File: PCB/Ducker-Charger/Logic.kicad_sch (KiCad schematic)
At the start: 30 parts, among them IC1 TPS54202HDDCT, J3 Debug, U2 STM32F401RBT6, Y1 16MHz

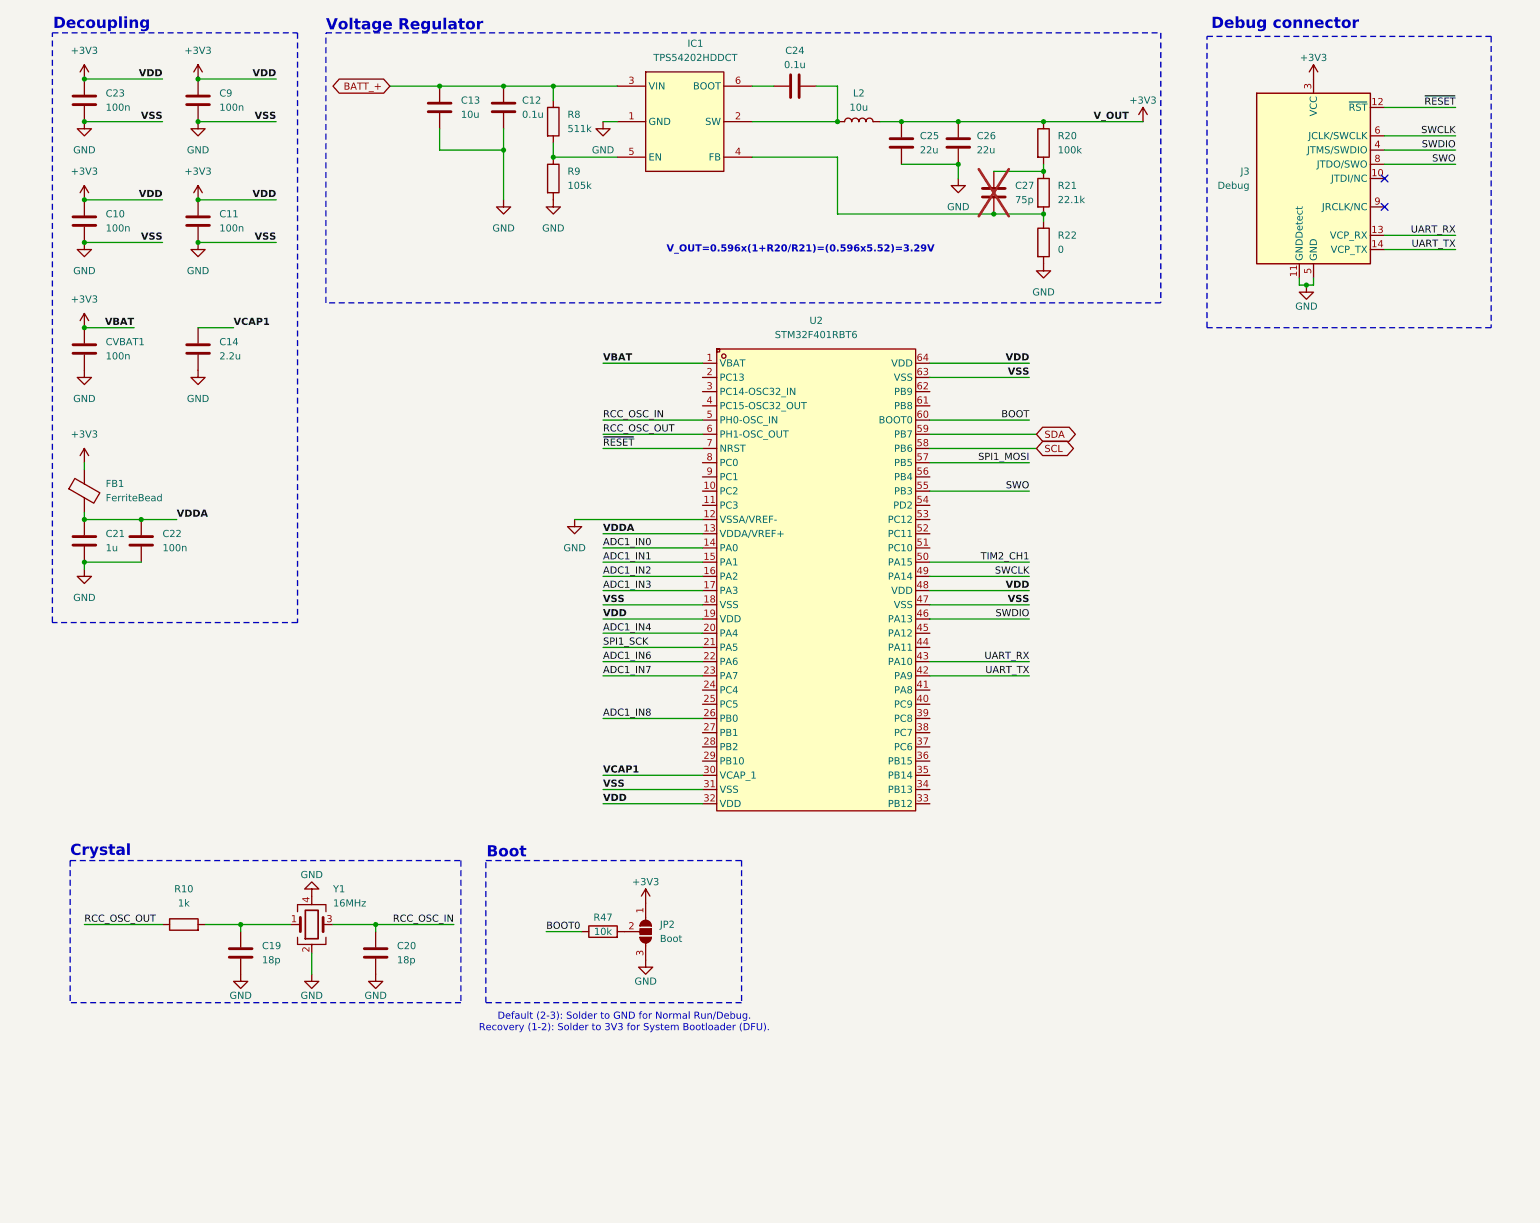
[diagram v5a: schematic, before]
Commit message: feat: progressed overall schematic
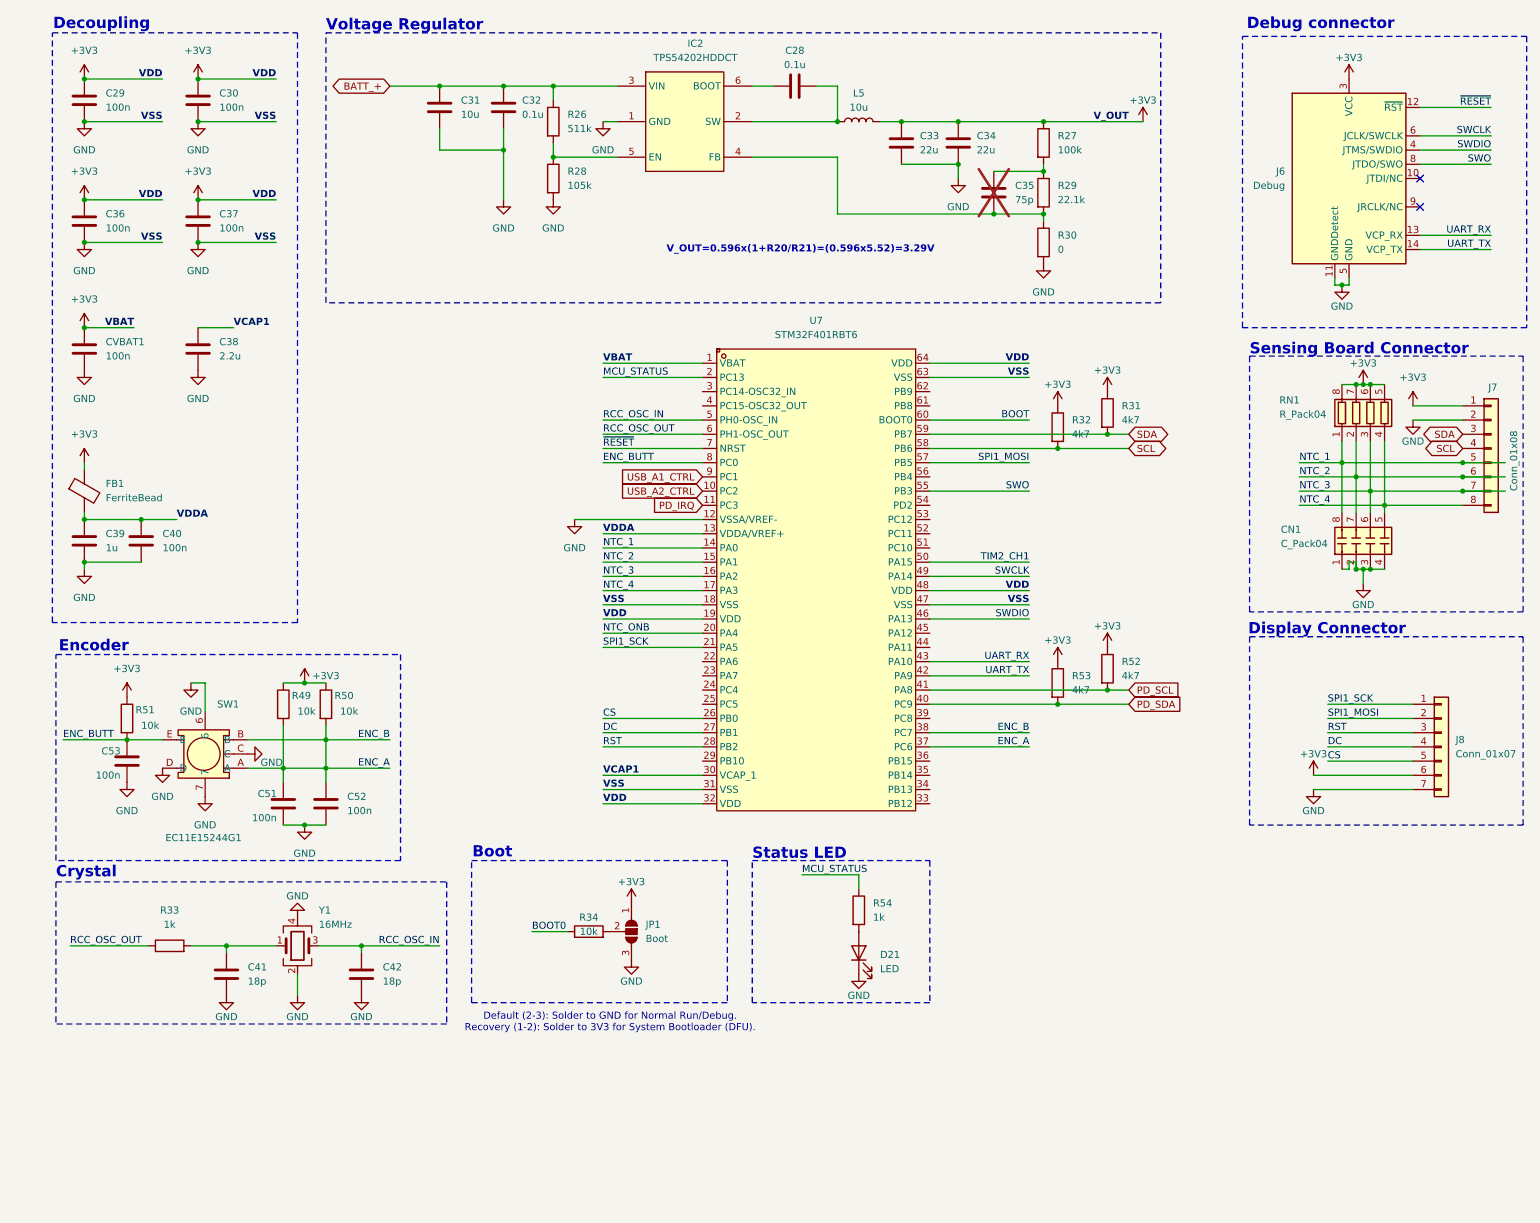
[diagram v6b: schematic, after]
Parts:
- added C51, C52, C53: 100n, symbol Device:C
- added CN1: C_Pack04, symbol Eagle_Main.:C_Pack04
- added D21: LED, LED_SMD:LED_0603_1608Metric, symbol Device:LED
- added J7: Conn_01x08, symbol Connector_Generic:Conn_01x08
- added J8: Conn_01x07, symbol Connector_Generic:Conn_01x07
- added R31, R32, R52, R53: 4k7, symbol Device:R
- added R49, R50, R51: 10k, symbol Device:R
- added R54: 1k, Resistor_SMD:R_0603_1608Metric, symbol Device:R
- added RN1: R_Pack04, symbol Device:R_Pack04
- added SW1: EC11E15244G1, EasyEDA:SW-TH_EC11E15244G1, symbol EasyEDA:EC11E15244G1
- IC2: renamed from IC1; footprint SOT95P280X110-6N -> TPS54202HDDCT:SOT95P280X110-6N
- renumbered C24 to C28, C23 to C29, C9 to C30, C13 to C31, C12 to C32, C25 to C33, C26 to C34, C27 to C35, C10 to C36, C11 to C37, C14 to C38, C21 to C39, C22 to C40, C19 to C41, C20 to C42, J3 to J6, JP2 to JP1, L2 to L5, R8 to R26, R20 to R27, R9 to R28, R21 to R29, R22 to R30, R10 to R33, R47 to R34, U2 to U7
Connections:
- net +3V3: now also J7.1 (Pin_1), J8.6 (Pin_6), R31.1, R32.1, R49.1, R50.1, R51.1, R52.1, R53.1, RN1.5 (R4.2), RN1.6 (R3.2), RN1.7 (R2.2), RN1.8 (R1.2)
- net GND: now also C51.2, C52.2, C53.2, CN1.1 (R1.1), CN1.2 (R2.1), CN1.3 (R3.1), CN1.4 (R4.1), D21.1 (K), J7.2 (Pin_2), J8.7 (Pin_7), SW1.6, SW1.7, SW1.C, SW1.D
- net SCL: now also J7.4 (Pin_4), R32.2
- net SDA: now also J7.3 (Pin_3), R31.2
- net SPI1_MOSI: now also J8.2 (Pin_2)
- net SPI1_SCK: now also J8.1 (Pin_1)
- net USB_A2_CTRL: now reaches U7.10 (PC2)
- net PD_IRQ: now reaches U7.11 (PC3)
- net MCU_STATUS: now reaches U7.2 (PC13)
- net MCU_STATUS: now also R54.1
- net DC: now reaches U7.27 (PB1)
- net DC: now also J8.4 (Pin_4)
- net RST: now reaches U7.28 (PB2)
- net RST: now also J8.3 (Pin_3)
- net ENC_A: now reaches U7.37 (PC6)
- net ENC_A: now also U7.38 (PC7), C51.1, C52.1, R49.2, R50.2, SW1.A, SW1.B
- net PD_SDA: now reaches U7.40 (PC9)
- net PD_SDA: now also R53.2
- net PD_SCL: now reaches U7.41 (PA8)
- net PD_SCL: now also R52.2
- net ENC_BUTT: now reaches U7.8 (PC0)
- net ENC_BUTT: now also C53.1, R51.2, SW1.E
- net USB_A1_CTRL: now reaches U7.9 (PC1)
- net ADC1_IN0 renamed NTC_1
- net NTC_1: now also CN1.8 (R1.2), J7.5 (Pin_5), RN1.1 (R1.1)
- net ADC1_IN1 renamed NTC_2
- net NTC_2: now also CN1.7 (R2.2), J7.6 (Pin_6), RN1.2 (R2.1)
- net ADC1_IN2 renamed NTC_3
- net NTC_3: now also CN1.6 (R3.2), J7.7 (Pin_7), RN1.3 (R3.1)
- net ADC1_IN3 renamed NTC_4
- net NTC_4: now also CN1.5 (R4.2), J7.8 (Pin_8), RN1.4 (R4.1)
- net ADC1_IN4 renamed NTC_ONB
- net ADC1_IN6: no longer names the net of U7.22 (PA6)
- net ADC1_IN7: no longer names the net of U7.23 (PA7)
- net ADC1_IN8 renamed CS
- net CS: now also J8.5 (Pin_5)
- new net: D21.2 (A), R54.2
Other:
- note added: "Display Connector"
- note added: "Encoder"
- note added: "Sensing Board Connector"
- note added: "Status LED"
- moved on the sheet: C41, C42, J6, JP1, R33, R34, Y1

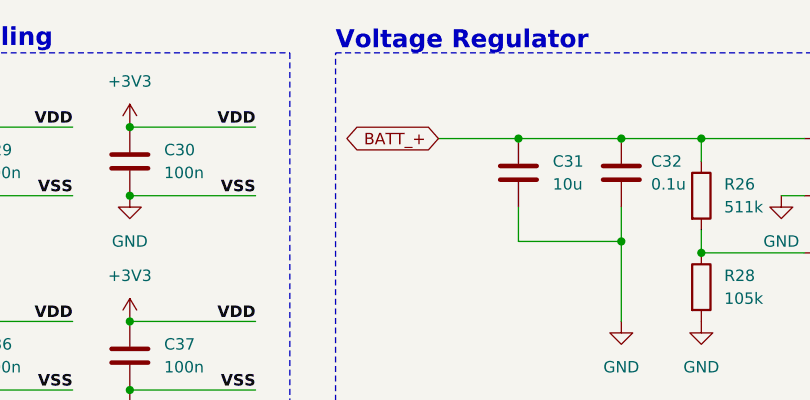
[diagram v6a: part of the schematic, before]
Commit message: fix: power symbols
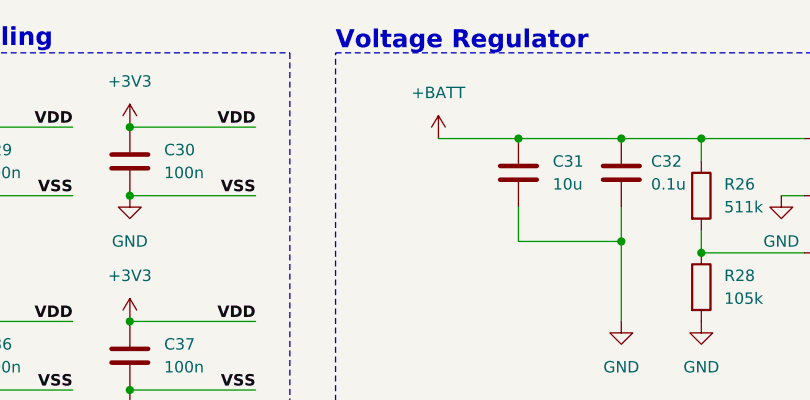
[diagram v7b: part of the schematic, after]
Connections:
- net BATT_+ renamed +BATT
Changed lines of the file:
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@@
 		)
 	)
-	(global_label "BATT_+"
-		(shape bidirectional)
-		(at 78.74 27.94 180)
-		(fields_autoplaced yes)
-		(effects
-			(font
-				(size 1.27 1.27)
-			)
-			(justify right)
-		)
-		(property "Intersheetrefs" "${INTERSHEET_REFS}"
-			(at 67.8097 27.94 0)
-			(effects
-				(font
-					(size 1.27 1.27)
-				)
-				(justify right)
-				(hide yes)
-			)
-		)
-	)
 	(global_label "PD_IRQ"
 		(shape input)
@@
 					(unit 1)
 				)
+			)
+		)
+	)
+	(symbol
+		(lib_id "power:+BATT")
+		(at 78.74 27.94 0)
+		(unit 1)
+		(exclude_from_sim no)
+		(in_bom yes)
+		(on_board yes)
+		(dnp no)
+		(fields_autoplaced yes)
+		(property "Reference" "#PWR0117"
+			(at 78.74 31.75 0)
+			(effects
+				(font
+					(size 1.27 1.27)
+				)
+				(hide yes)
+			)
+		)
+		(property "Value" "+BATT"
+			(at 78.74 22.86 0)
+			(effects
+				(font
+					(size 1.27 1.27)
+				)
+			)
+		)
+		(property "Footprint" ""
+			(at 78.74 27.94 0)
+			(effects
+				(font
+					(size 1.27 1.27)
+				)
+				(hide yes)
+			)
+		)
+		(property "Datasheet" ""
+			(at 78.74 27.94 0)
+			(effects
+				(font
+					(size 1.27 1.27)
+				)
+				(hide yes)
+			)
+		)
+		(property "Description" "Power symbol creates a global label with name \"+BATT\""
+			(at 78.74 27.94 0)
+			(effects
+				(font
+					(size 1.27 1.27)
+				)
+				(hide yes)
+			)
+		)
+		(pin "1"
+		)
+		(instances
+			(project "Ducker-Charger"
+				(path "/74790d6c-a68e-4e6d-b4a9-43de1843f817/b1375a06-d47d-478c-835c-6ba88db99bcf"
+					(reference "#PWR0117")
+					(unit 1)
+				)

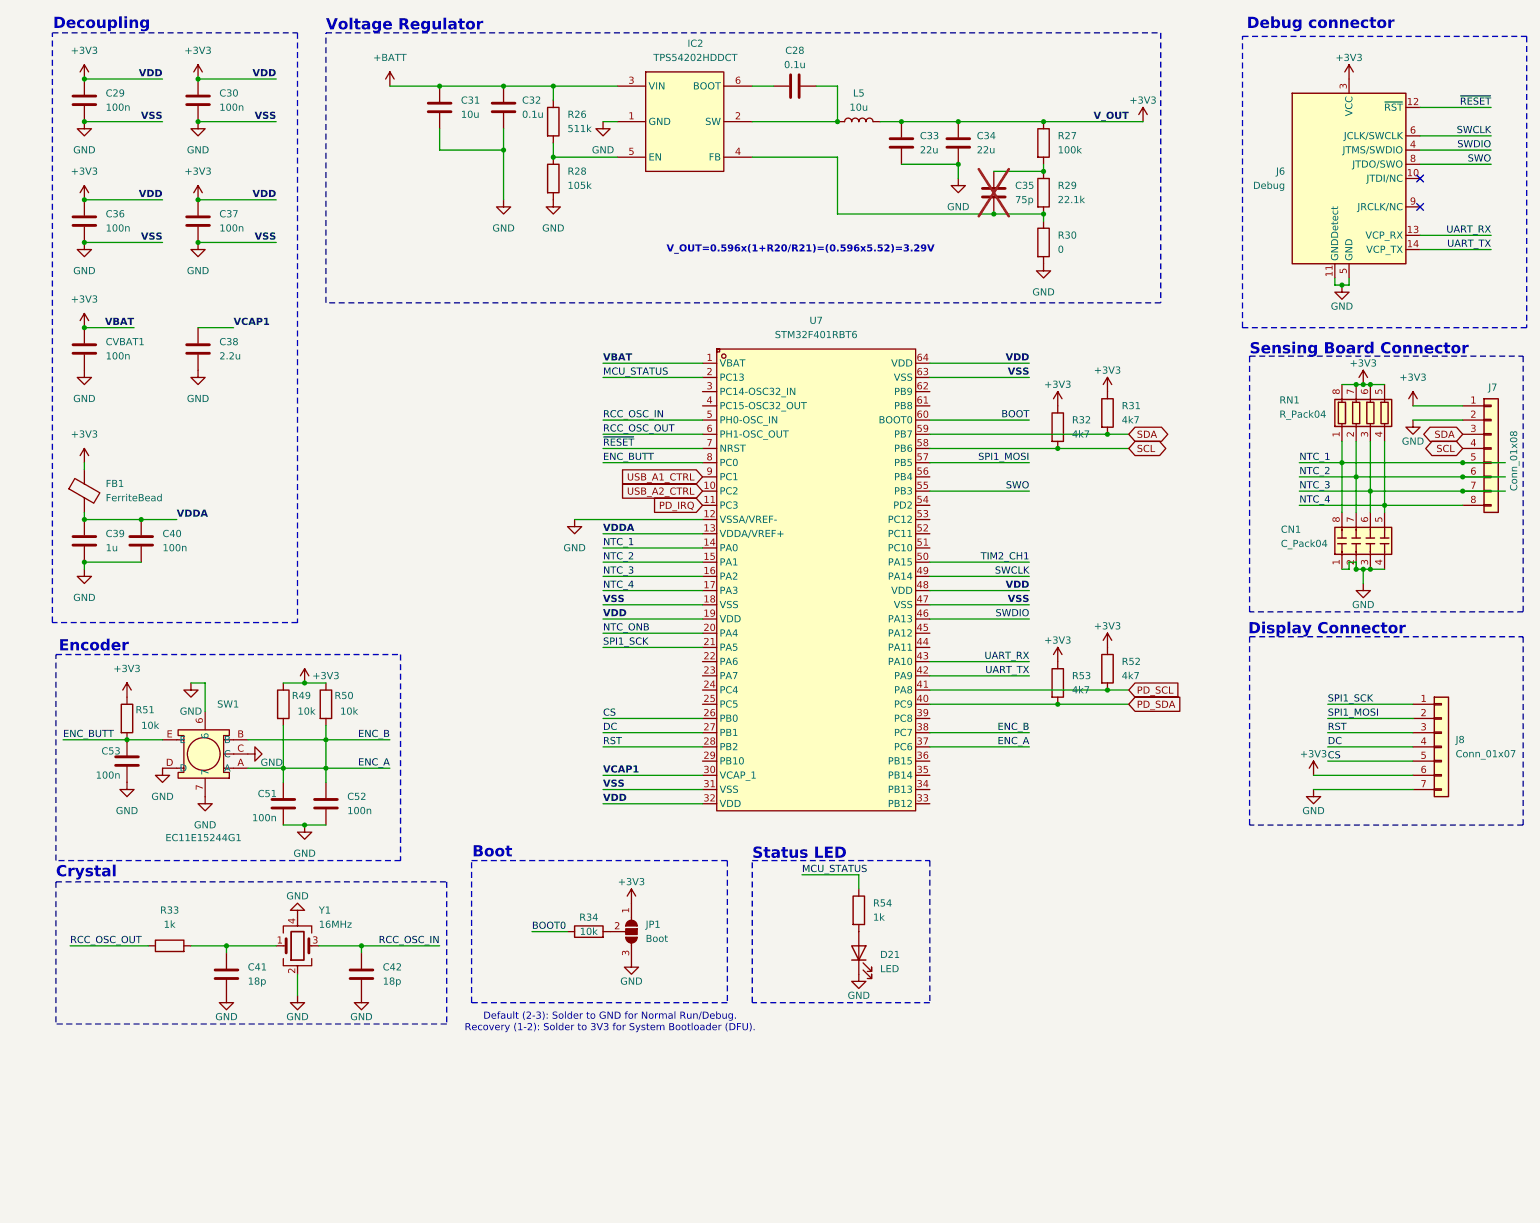
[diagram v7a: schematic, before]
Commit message: fix: I2C is now a BUS, no longer a global label
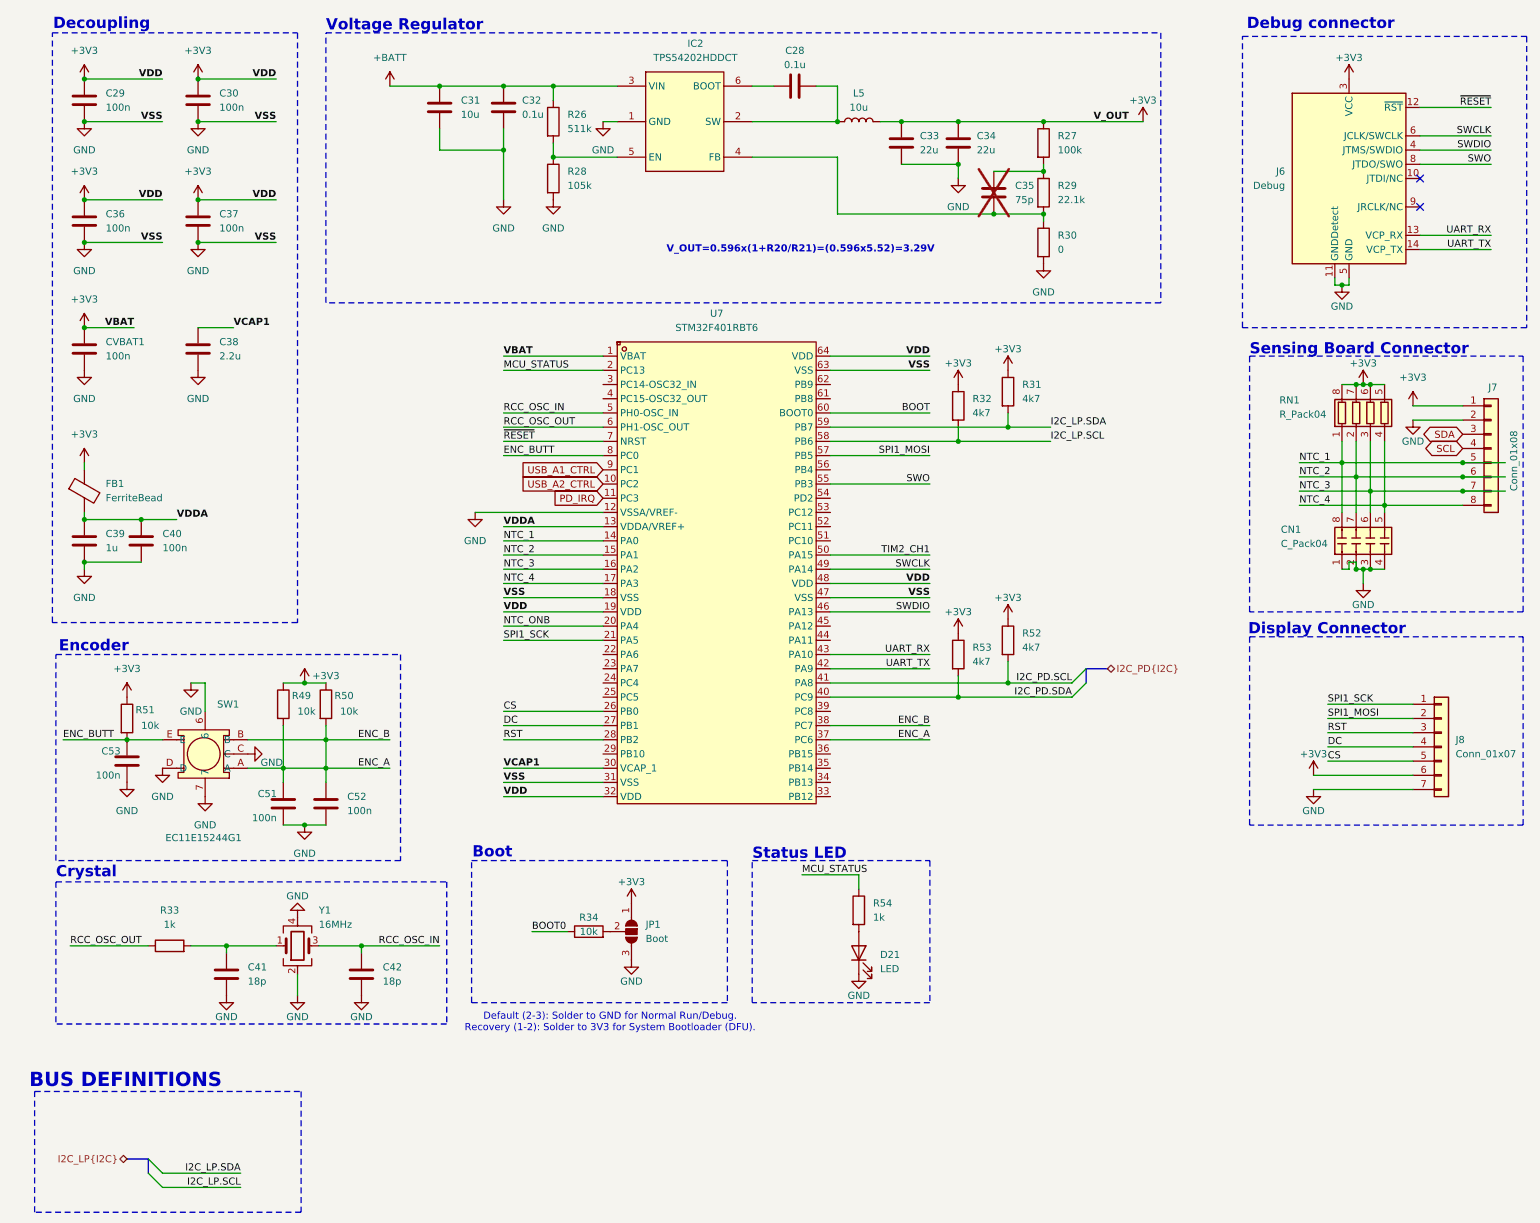
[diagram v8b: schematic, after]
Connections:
- net SCL: no longer R32.2, U7.58 (PB6)
- net SDA: no longer R31.2, U7.59 (PB7)
- net PD_SCL renamed I2C_PD.SCL
- net PD_SDA renamed I2C_PD.SDA
- new net I2C_LP.SCL: R32.2, U7.58 (PB6)
- new net I2C_LP.SDA: R31.2, U7.59 (PB7)
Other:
- note added: "BUS DEFINITIONS"
- moved on the sheet: R31, R32, R52, R53, U7
